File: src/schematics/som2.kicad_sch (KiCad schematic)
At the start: 1 part, among them J2 DDR4_SODIMM_Board

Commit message: Add component footprints
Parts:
- J2: footprint (none) -> ECAP5-BCARRIER-XLITE:SODIMM-260_DDR4_H4.0-5.2_OrientationStd_Socket; Part (none) -> 2309407-2
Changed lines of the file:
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@@
 			)
 		)
-		(property "Footprint" ""
+		(property "Footprint" "ECAP5-BCARRIER-XLITE:SODIMM-260_DDR4_H4.0-5.2_OrientationStd_Socket"
 			(at 231.14 58.42 0)
 			(effects
@@
 		(property "Description" ""
 			(at 231.14 58.42 0)
+			(effects
+				(font
+					(size 1.27 1.27)
+				)
+				(hide yes)
+			)
+		)
+		(property "Part" "2309407-2"
+			(at 250.19 95.25 0)
 			(effects
 				(font
@@
 			)
 		)
-		(property "Footprint" ""
+		(property "Footprint" "ECAP5-BCARRIER-XLITE:SODIMM-260_DDR4_H4.0-5.2_OrientationStd_Socket"
 			(at 166.37 58.42 0)
 			(effects
@@
 		(property "Description" ""
 			(at 166.37 58.42 0)
+			(effects
+				(font
+					(size 1.27 1.27)
+				)
+				(hide yes)
+			)
+		)
+		(property "Part" "2309407-2"
+			(at 185.42 95.25 0)
 			(effects
 				(font
@@
 			)
 		)
-		(property "Footprint" ""
+		(property "Footprint" "ECAP5-BCARRIER-XLITE:SODIMM-260_DDR4_H4.0-5.2_OrientationStd_Socket"
 			(at 101.6 58.42 0)
 			(effects
@@
 		(property "Description" ""
 			(at 101.6 58.42 0)
+			(effects
+				(font
+					(size 1.27 1.27)
+				)
+				(hide yes)
+			)
+		)
+		(property "Part" "2309407-2"
+			(at 120.65 95.25 0)
 			(effects
 				(font
@@
 			)
 		)
-		(property "Footprint" ""
+		(property "Footprint" "ECAP5-BCARRIER-XLITE:SODIMM-260_DDR4_H4.0-5.2_OrientationStd_Socket"
 			(at 29.21 58.42 0)
 			(effects
@@
 			(effects
 				(font
+					(size 1.27 1.27)
+				)
+				(hide yes)
+			)
+		)
+		(property "Part" "2309407-2"
+			(at 48.26 95.25 0)
+			(effects
+				(font

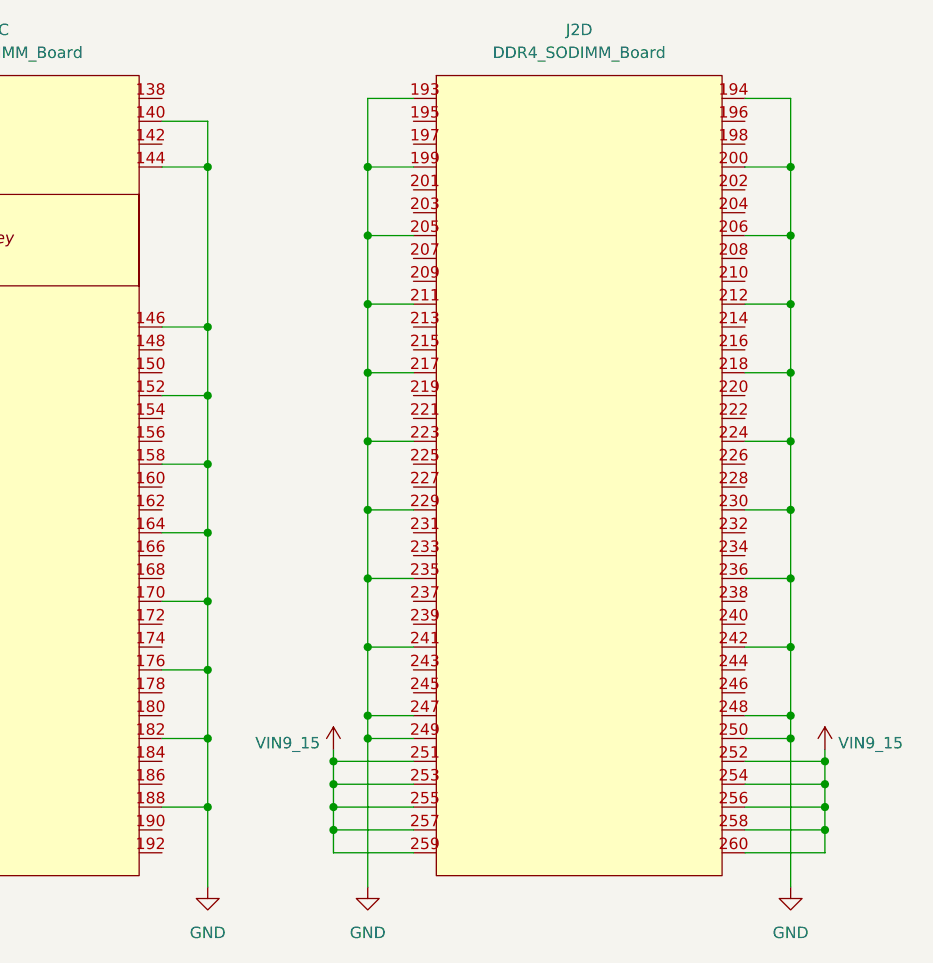
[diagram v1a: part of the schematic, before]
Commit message: Route the LVDS pairs
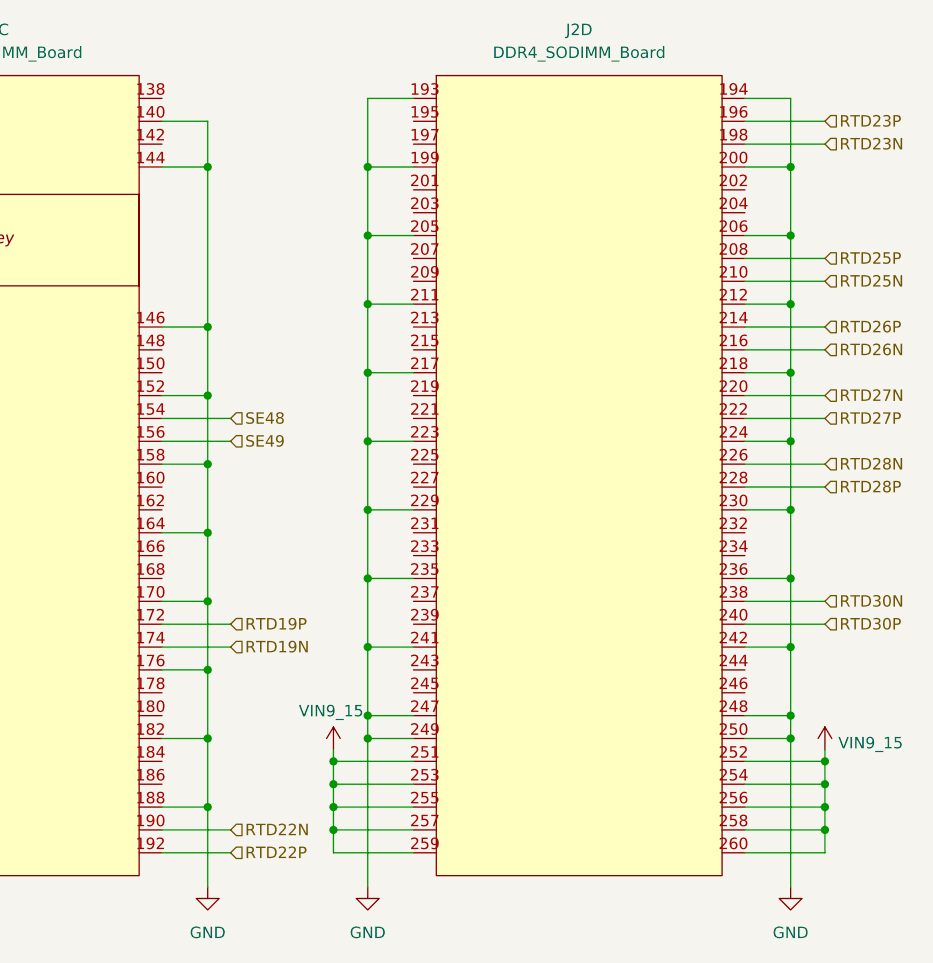
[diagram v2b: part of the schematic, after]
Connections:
- net RTD23P: now reaches J2.196
- net RTD23N: now reaches J2.198
- net RTD25P: now reaches J2.208
- net RTD25N: now reaches J2.210
- net RTD26P: now reaches J2.214
- net RTD26N: now reaches J2.216
- net RTD27N: now reaches J2.220
- net RTD27P: now reaches J2.222
- net RTD28N: now reaches J2.226
- net RTD28P: now reaches J2.228
- net RTD30N: now reaches J2.238
- net RTD30P: now reaches J2.240
- net SE48: now reaches J2.154
- net SE49: now reaches J2.156
- net RTD19P: now reaches J2.172
- net RTD19N: now reaches J2.174
- net RTD22N: now reaches J2.190
- net RTD22P: now reaches J2.192

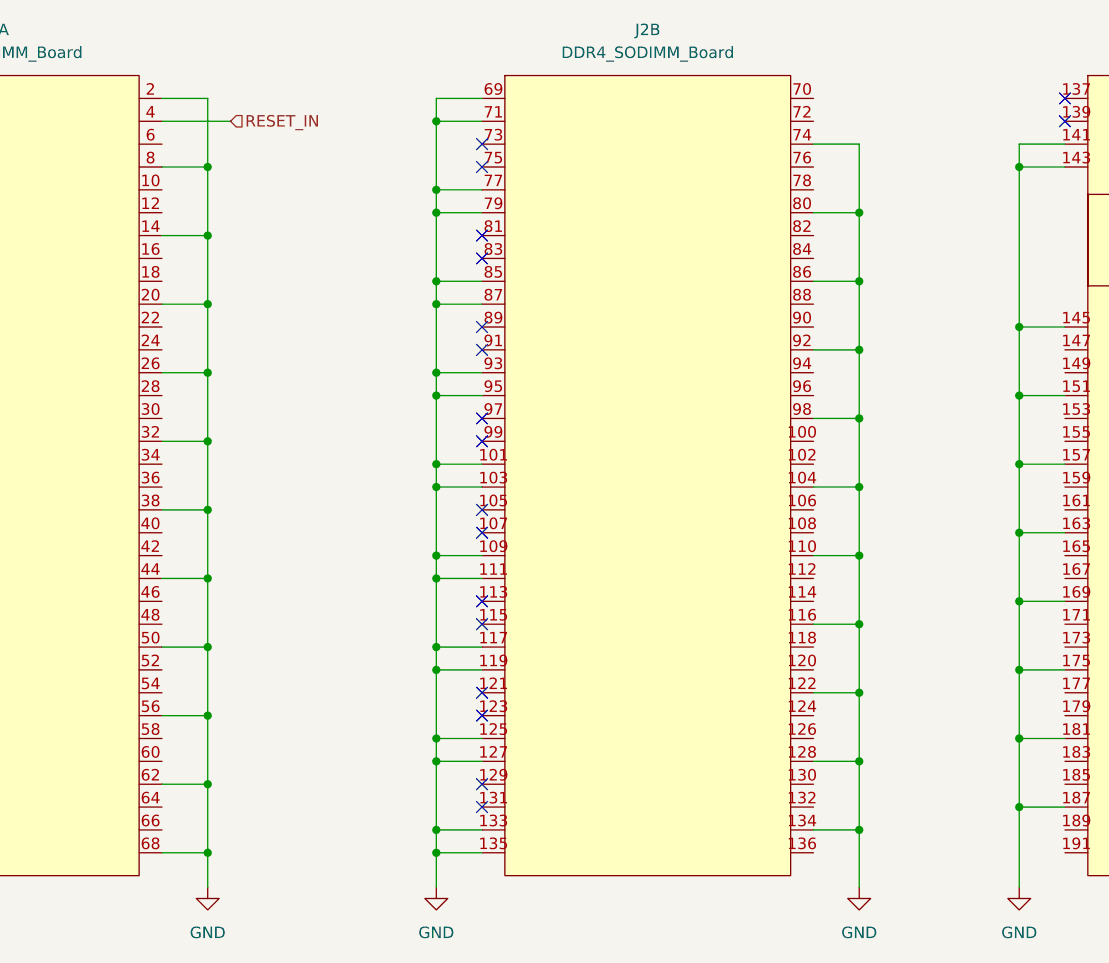
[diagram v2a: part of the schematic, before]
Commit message: Finish routing the single-ended signals
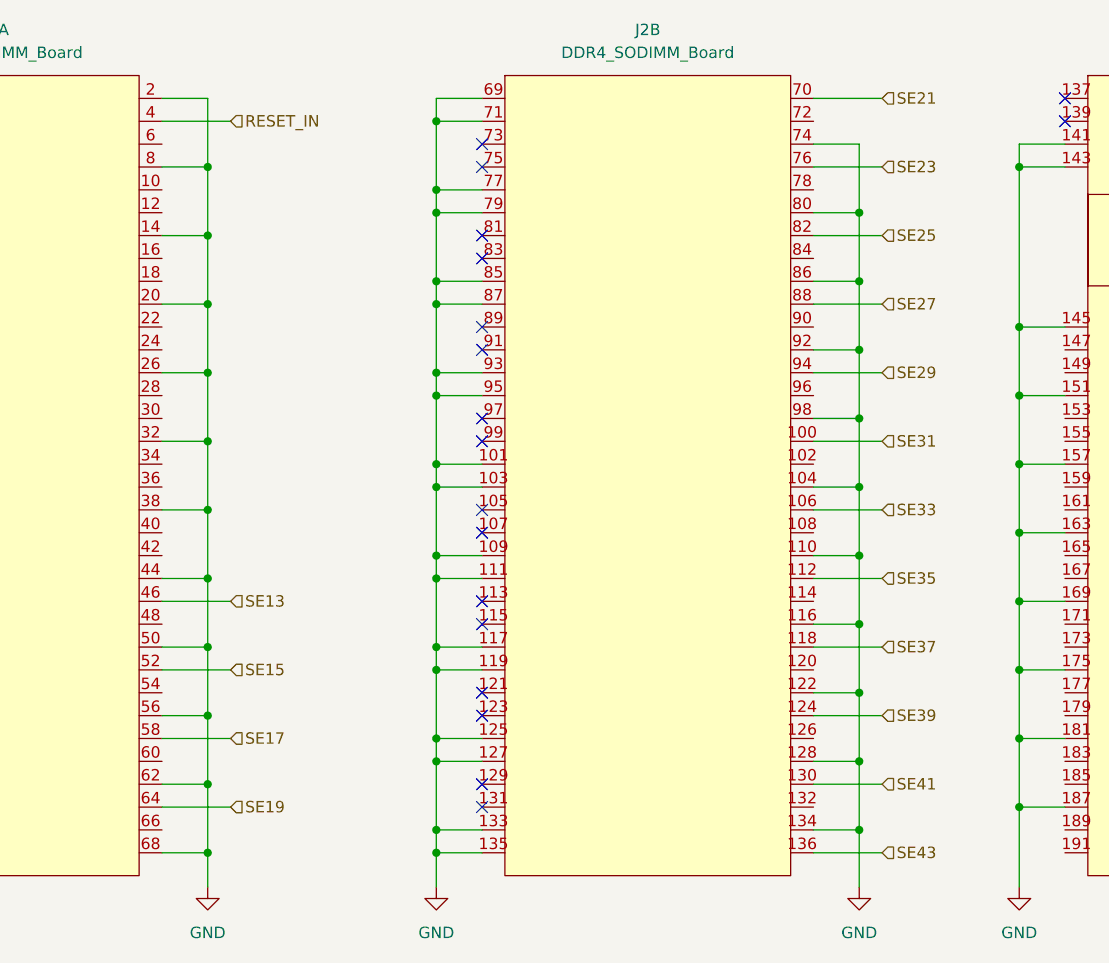
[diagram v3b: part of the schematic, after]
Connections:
- net SE31: now reaches J2.100
- net SE33: now reaches J2.106
- net SE35: now reaches J2.112
- net SE37: now reaches J2.118
- net SE39: now reaches J2.124
- net SE41: now reaches J2.130
- net SE43: now reaches J2.136
- net SE21: now reaches J2.70
- net SE23: now reaches J2.76
- net SE25: now reaches J2.82
- net SE27: now reaches J2.88
- net SE29: now reaches J2.94
- net SE13: now reaches J2.46
- net SE15: now reaches J2.52
- net SE17: now reaches J2.58
- net SE19: now reaches J2.64

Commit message: Fix erc issues
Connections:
- no-connect marks 20 -> 116

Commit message: Improve the schematic
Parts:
- J2: MPN (none) -> 2309407-1; now in the parts list
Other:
- title: (none) -> ECAP5-BCARRIER-XLITE
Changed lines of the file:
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@@
 	(generator_version "9.0")
 	(paper "A4")
+	(title_block
+		(title "ECAP5-BCARRIER-XLITE")
+		(date "2025-09-21")
+		(rev "1.0")
+		(comment 1 "ECAP5")
+		(comment 2 "SOM2")
+	)
 	(junction
 		(at 161.29 124.46)
@@
 		(unit 4)
 		(exclude_from_sim no)
-		(in_bom no)
+		(in_bom yes)
 		(on_board yes)
 		(dnp no)
@@
 			)
 		)
+		(property "MPN" "2309407-1"
+			(at 250.19 95.25 0)
+			(effects
+				(font
+					(size 1.27 1.27)
+				)
+				(hide yes)
+			)
+		)
 		(pin "9"
 		)
@@
 		(unit 3)
 		(exclude_from_sim no)
-		(in_bom no)
+		(in_bom yes)
 		(on_board yes)
 		(dnp no)
@@
 			)
 		)
+		(property "MPN" "2309407-1"
+			(at 185.42 95.25 0)
+			(effects
+				(font
+					(size 1.27 1.27)
+				)
+				(hide yes)
+			)
+		)
 		(pin "9"
 		)
@@
 		(unit 2)
 		(exclude_from_sim no)
-		(in_bom no)
+		(in_bom yes)
 		(on_board yes)
 		(dnp no)
@@
 			)
 		)
+		(property "MPN" "2309407-1"
+			(at 120.65 95.25 0)
+			(effects
+				(font
+					(size 1.27 1.27)
+				)
+				(hide yes)
+			)
+		)
 		(pin "9"
 		)
@@
 		(unit 1)
 		(exclude_from_sim no)
-		(in_bom no)
+		(in_bom yes)
 		(on_board yes)
 		(dnp no)
@@
 			(at 48.26 95.25 0)
 			(effects
+				(font
+					(size 1.27 1.27)
+				)
+				(hide yes)
+			)
+		)
+		(property "MPN" "2309407-1"
+			(at 48.26 95.25 0)
+			(effects
